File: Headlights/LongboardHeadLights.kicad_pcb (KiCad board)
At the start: 2 copper layers, 76.2 x 12.7 mm, 16 parts, among them P1 CONN_01X03, U1 AL8805

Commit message: updated project and completed rev 1 PCB
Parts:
- moved C2 6.55 mm to (155.1, 88.8), turned to 0 degrees
- moved C1 5.86 mm to (155.1, 90.7), turned to 0 degrees
- moved D3 2.36 mm to (196.6, 91.5)
- moved C5 2.29 mm to (196.6, 87.7)
- moved C4 1.87 mm to (180.1, 87.7)
- moved D2 1.47 mm to (180.2, 91.5)
- moved P1 1.35 mm to (130.4, 89.1)
- moved D1 0.64 mm to (163.8, 91.5)
- moved C3 0.31 mm to (163.8, 87.7)
- moved R1 0.25 mm to (153.6, 93.7)
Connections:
- D1 pad 3: (no net) -> GND
- D2 pad 3: (no net) -> GND
- D3 pad 3: (no net) -> GND
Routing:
- net GND: track 6.38 -> 137.1 mm, vias 3 -> 67
- net VCC: track 30.1 -> 37.8 mm
- net Net-(C5-Pad2): track 77.3 -> 74.7 mm
- net Net-(C3-Pad2): track 20.5 -> 22.0 mm
- net Net-(C4-Pad2): track 20.9 -> 22.2 mm
- net Net-(C3-Pad1): track 16.4 -> 17.0 mm
- added copper zone on F.Cu, net GND
- added copper zone on F.Cu, net VCC
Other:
- board size 76.2 x 12.7 mm -> 76.2 x 10.8 mm

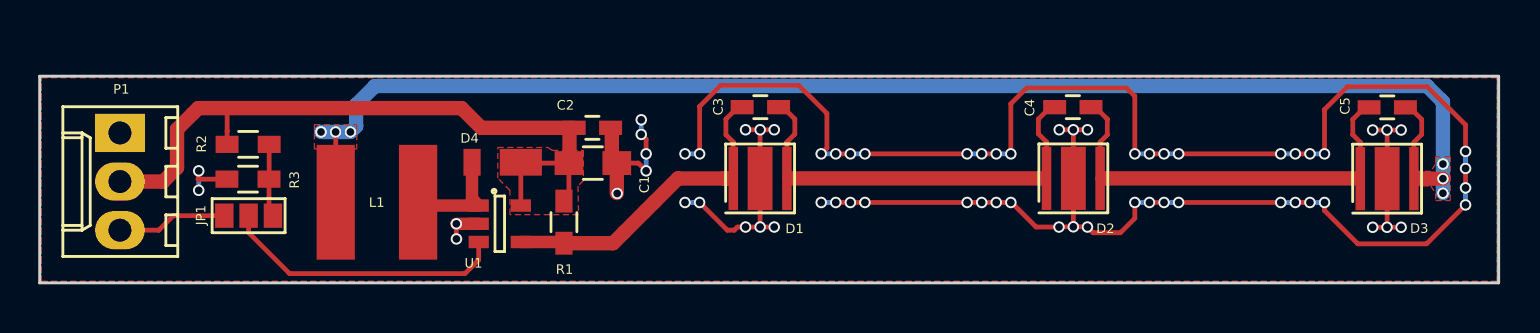
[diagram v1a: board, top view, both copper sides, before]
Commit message: finished PCB, updating plan
ditched tail light turn signal idea, now only need one PCB and just
switch out LEDs
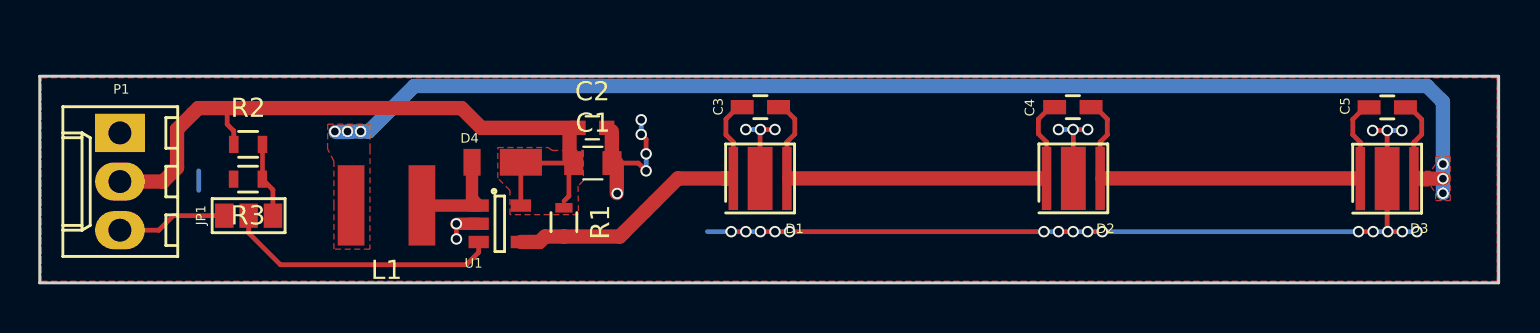
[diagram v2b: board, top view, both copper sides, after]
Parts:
- C1: footprint Capacitors_SMD:C_0805_HandSoldering -> Capacitors_SMD:C_0805
- C2: footprint Capacitors_SMD:C_0603_HandSoldering -> Capacitors_SMD:C_0603
- L1: footprint Light_Parts:Inductor_Bourns_6045 -> Light_Parts:Inductor5x5
- R1, R2, R3: footprint Resistors_SMD:R_0603_HandSoldering -> Resistors_SMD:R_0603
- moved L1 2.66 mm to (144.3, 92.9)
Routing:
- net GND: track 137.1 -> 62.9 mm, vias 67 -> 31
- net Net-(C5-Pad2): track 74.7 -> 69.8 mm
- net (no net): track 0.00 -> 1.02 mm
- net /CTRL: track 15.0 -> 14.4 mm

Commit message: couple quick changes
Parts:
- R1: value 0.275 -> 0.3
- R2: value 6200 -> 38000
- R3: value 1600 -> 10000
- moved C2 0.42 mm to (154.6, 88.8)
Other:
- board text added: "GiS ENGINEERING MG"
- board text added: "REVISION 1 2/17"
- board text added: "WARNING: BRIGHT!"
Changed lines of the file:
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@@
 (kicad_pcb (version 4) (host pcbnew 4.0.2-stable)
   (general
-    (links 27)
-    (no_connects 6)
-    (area 114.910601 85.7861 202.465001 102.839501)
+    (links 30)
+    (no_connects 0)
+    (area 126.114999 86.039999 202.465001 96.985001)
     (thickness 1.6)
-    (drawings 6)
+    (drawings 9)
     (tracks 181)
     (zones 0)
@@
   (page A4)
   (layers
-    (0 F.Cu signal)
+    (0 F.Cu signal hide)
     (31 B.Cu signal hide)
     (32 B.Adhes user)
@@
     (tags "resistor 0603")
     (attr smd)
-    (fp_text reference R2 (at 0 -1.9) (layer F.SilkS)
-      (effects (font (size 1 1) (thickness 0.15)))
-    )
-    (fp_text value 6200 (at 0 1.9) (layer F.Fab)
-      (effects (font (size 1 1) (thickness 0.15)))
+    (fp_text reference R2 (at -1.693 0.0378 90) (layer F.SilkS)
+      (effects (font (size 0.5 0.5) (thickness 0.125)))
+    )
+    (fp_text value 38000 (at 2.5488 1.8158 180) (layer F.Fab)
+      (effects (font (size 0.5 0.5) (thickness 0.125)))
     )
     (fp_line (start -0.8 0.4) (end -0.8 -0.4) (layer F.Fab) (width 0.1))
@@
     (tags "resistor 0603")
     (attr smd)
-    (fp_text reference R3 (at 0 -1.9 180) (layer F.SilkS)
-      (effects (font (size 1 1) (thickness 0.15)))
-    )
-    (fp_text value 1600 (at 0 1.9 180) (layer F.Fab)
-      (effects (font (size 1 1) (thickness 0.15)))
+    (fp_text reference R3 (at 1.684406 0.001466 270) (layer F.SilkS)
+      (effects (font (size 0.5 0.5) (thickness 0.125)))
+    )
+    (fp_text value 10000 (at -2.455794 1.804866 360) (layer F.Fab)
+      (effects (font (size 0.5 0.5) (thickness 0.125)))
     )
     (fp_line (start -0.8 0.4) (end -0.8 -0.4) (layer F.Fab) (width 0.1))
@@
   )
   (module Capacitors_SMD:C_0603 (layer F.Cu)
-    (at 155.0543 88.8111)
+    (at 154.6352 88.8111)
     (descr "Capacitor SMD 0603, reflow soldering, AVX (see smccp.pdf)")
     (tags "capacitor 0603")
     (attr smd)
-    (fp_text reference C2 (at 0 -1.9) (layer F.SilkS)
-      (effects (font (size 1 1) (thickness 0.15)))
-    )
-    (fp_text value 2.2uF (at 0 -1.6129) (layer F.Fab)
-      (effects (font (size 1 1) (thickness 0.15)))
+    (fp_text reference C2 (at -1.0033 -1.1557) (layer F.SilkS)
+      (effects (font (size 0.5 0.5) (thickness 0.125)))
+    )
+    (fp_text value 2.2uF (at 1.9177 -0.4445 90) (layer F.Fab)
+      (effects (font (size 0.5 0.5) (thickness 0.125)))
     )
     (fp_line (start -0.8 0.4) (end -0.8 -0.4) (layer F.Fab) (width 0.1))
@@
     (tags "capacitor 0805")
     (attr smd)
-    (fp_text reference C1 (at 0 -2.1) (layer F.SilkS)
-      (effects (font (size 1 1) (thickness 0.15)))
-    )
-    (fp_text value 4.7uF (at 0 2.1) (layer F.Fab)
-      (effects (font (size 1 1) (thickness 0.15)))
+    (fp_text reference C1 (at -1.3589 1.4224 180) (layer F.SilkS)
+      (effects (font (size 0.5 0.5) (thickness 0.125)))
+    )
+    (fp_text value 4.7uF (at 0.7747 1.4224) (layer F.Fab)
+      (effects (font (size 0.5 0.5) (thickness 0.125)))
     )
     (fp_line (start -1 0.625) (end -1 -0.625) (layer F.Fab) (width 0.1))
@@
     (tags "resistor 0603")
     (attr smd)
-    (fp_text reference R1 (at 0 -1.9 270) (layer F.SilkS)
-      (effects (font (size 1 1) (thickness 0.15)))
-    )
-    (fp_text value 0.275 (at 0 1.9 270) (layer F.Fab)
-      (effects (font (size 1 1) (thickness 0.15)))
+    (fp_text reference R1 (at 0.8763 -1.2446 270) (layer F.SilkS)
+      (effects (font (size 0.5 0.5) (thickness 0.125)))
+    )
+    (fp_text value 0.3 (at 1.7145 0.0254 360) (layer F.Fab)
+      (effects (font (size 0.5 0.5) (thickness 0.125)))
     )
     (fp_line (start -0.8 0.4) (end -0.8 -0.4) (layer F.Fab) (width 0.1))
@@
   (module Light_Parts:Inductor5x5 (layer F.Cu)
     (at 144.3016 92.8624)
-    (fp_text reference L1 (at 0 3.3782) (layer F.SilkS)
-      (effects (font (size 1 1) (thickness 0.15)))
-    )
-    (fp_text value INDUCTOR (at 0.7832 -3.6322) (layer F.Fab)
-      (effects (font (size 1 1) (thickness 0.15)))
+    (fp_text reference L1 (at -1.8584 2.8702) (layer F.SilkS)
+      (effects (font (size 0.5 0.5) (thickness 0.125)))
+    )
+    (fp_text value INDUCTOR (at 0.0974 -2.8702) (layer F.Fab)
+      (effects (font (size 0.5 0.5) (thickness 0.125)))
     )
     (pad 1 smd rect (at -1.85 0) (size 1.4 4.2) (layers F.Cu F.Paste F.Mask)
@@
       (net 7 "Net-(D4-Pad2)"))
   )
+  (gr_text "WARNING: BRIGHT!" (at 179.9336 95.5548) (layer F.SilkS)
+    (effects (font (size 0.75 0.75) (thickness 0.1875)))
+  )
+  (gr_text "REVISION 1\n2/17" (at 199.9234 95.6056) (layer F.SilkS)
+    (effects (font (size 0.5 0.5) (thickness 0.125)))
+  )
+  (gr_text "GiS ENGINEERING\nMG" (at 194.1322 95.6056) (layer F.SilkS)
+    (effects (font (size 0.5 0.5) (thickness 0.125)))
+  )
   (dimension 10.7696 (width 0.3) (layer Dwgs.User)

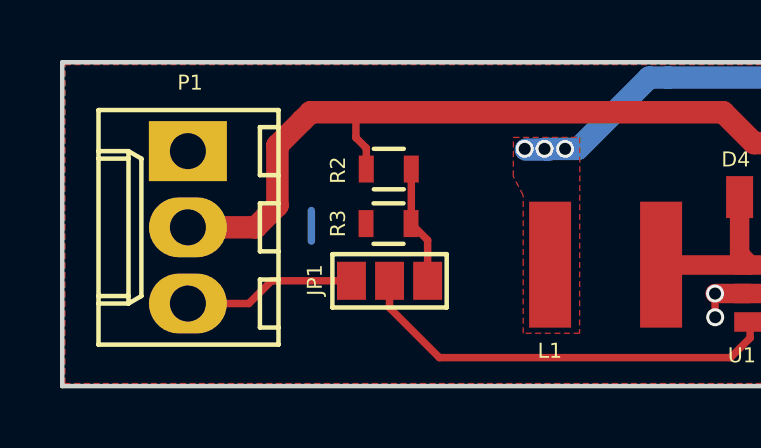
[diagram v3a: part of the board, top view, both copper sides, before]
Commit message: fixed a bad trace
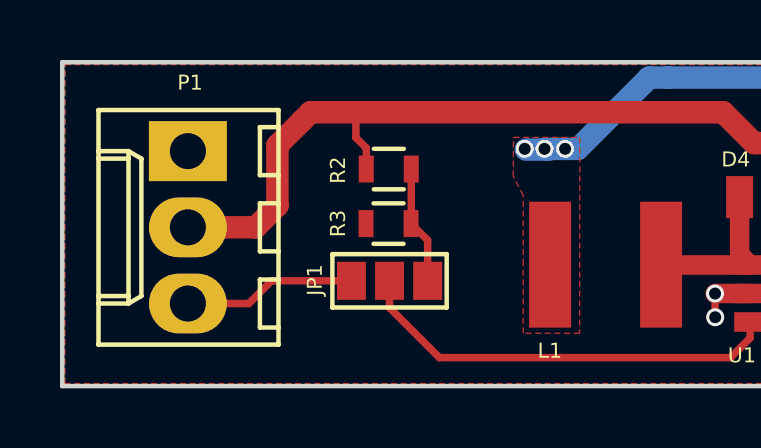
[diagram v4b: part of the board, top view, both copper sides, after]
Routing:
- net (no net): track 1.02 -> 0.00 mm
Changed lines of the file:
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@@
     (links 30)
     (no_connects 0)
-    (area 126.114999 86.039999 202.465001 96.985001)
+    (area 114.910601 86.039999 202.465001 102.839501)
     (thickness 1.6)
     (drawings 9)
-    (tracks 181)
+    (tracks 180)
     (zones 0)
     (modules 16)
@@
   (layers
     (0 F.Cu signal hide)
-    (31 B.Cu signal hide)
+    (31 B.Cu signal)
     (32 B.Adhes user)
     (33 F.Adhes user)
@@
   (gr_line (start 202.39 86.115) (end 126.19 86.115) (layer Edge.Cuts) (width 0.15))
   (gr_line (start 202.39 86.115) (end 202.39 96.91) (layer Edge.Cuts) (width 0.15))
-  (segment (start 134.493 91.059) (end 134.493 92.075) (width 0.25) (layer B.Cu) (net 0))
   (segment (start 136.325 89.675) (end 136.325 88.975) (width 0.25) (layer F.Cu) (net 1))
   (segment (start 136.325 88.975) (end 135.9789 88.6289) (width 0.25) (layer F.Cu) (net 1))

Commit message: yet another fix
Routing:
- net GND: track 62.9 -> 61.6 mm
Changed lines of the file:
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@@
     (thickness 1.6)
     (drawings 9)
-    (tracks 180)
+    (tracks 179)
     (zones 0)
     (modules 16)
@@
   (page A4)
   (layers
-    (0 F.Cu signal hide)
-    (31 B.Cu signal)
+    (0 F.Cu signal)
+    (31 B.Cu signal hide)
     (32 B.Adhes user)
     (33 F.Adhes user)
@@
   (segment (start 134.4682 87.7824) (end 134.195849 88.054751) (width 0.75) (layer F.Cu) (net 1))
   (segment (start 149.2504 88.8111) (end 148.2217 87.7824) (width 0.75) (layer F.Cu) (net 1))
-  (segment (start 154.1043 88.8111) (end 149.2504 88.8111) (width 0.75) (layer F.Cu) (net 1))
+  (segment (start 153.75 88.8111) (end 149.2504 88.8111) (width 0.75) (layer F.Cu) (net 1))
   (segment (start 134.195849 88.054751) (end 134.195849 88.054151) (width 0.25) (layer F.Cu) (net 1))
   (segment (start 133.3627 90.8939) (end 133.3627 88.8879) (width 0.75) (layer F.Cu) (net 1))
@@
   (segment (start 156.3297 92.2201) (end 156.3497 92.2401) (width 0.25) (layer F.Cu) (net 2))
   (via (at 156.3497 92.2401) (size 0.6) (drill 0.4) (layers F.Cu B.Cu) (net 2))
-  (segment (start 156.0703 88.9841) (end 156.0703 90.297) (width 0.75) (layer F.Cu) (net 2))
   (segment (start 149.117764 93.823146) (end 147.951854 93.823146) (width 0.65) (layer F.Cu) (net 2))
   (segment (start 147.951854 93.823146) (end 147.95 93.825) (width 0.25) (layer F.Cu) (net 2))
